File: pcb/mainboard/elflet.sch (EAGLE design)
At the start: 37 parts, among them J1 ZX62-B-5PA(33), J2 2212S-10SG-36, J3 STD-PINHD-1X6, Q1 IRLML6344TRPBF, Q2 ALS-PT19-315C_L177_TR8, SW1 SKRPACE010, U1 ESP-WROOM-32, U2 ADP3338AKCZ-3.3, U3 OSRB38C9AA, U4 BME280

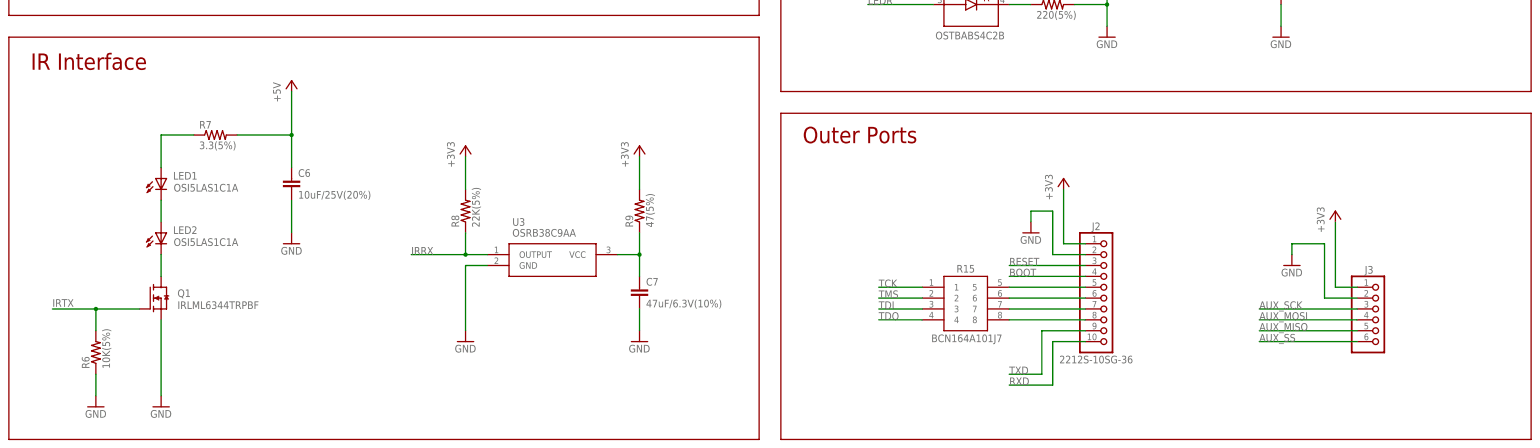
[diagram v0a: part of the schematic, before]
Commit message: place all parts on a board
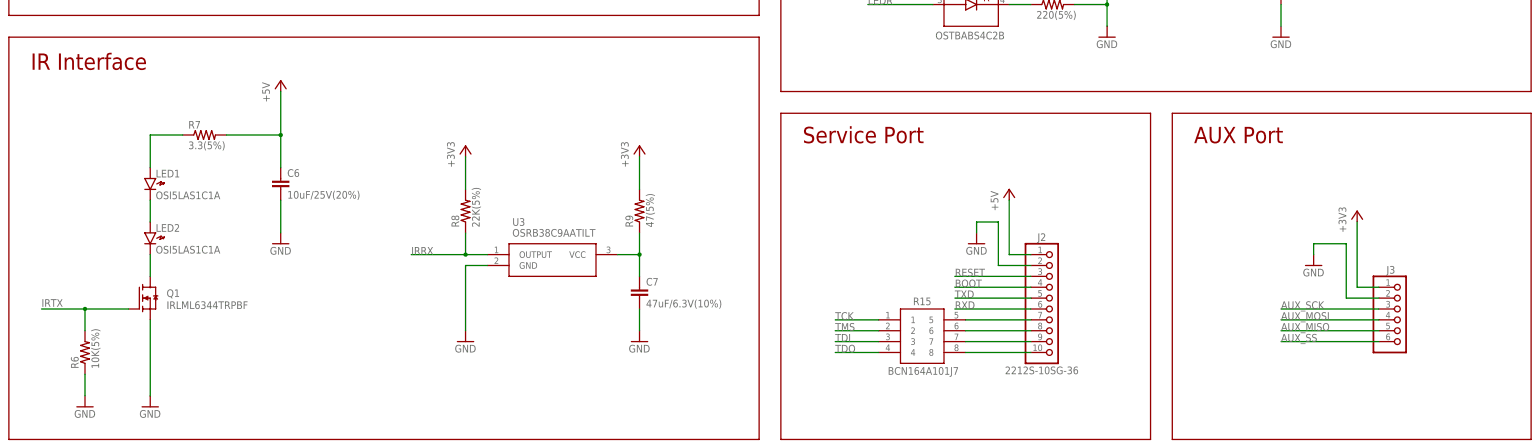
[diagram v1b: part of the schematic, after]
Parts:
- LED1, LED2: device led:LEDP-LCC-2 -> gen-discrete:LEDPLCC-2
- U3: value OSRB38C9AA -> OSRB38C9AATILT; device OSRB38C9AA:OSRB38C9AA -> OSRB38C9AA:OSRB38C9AATILT
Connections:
- net +3V3: no longer J2.1
- net +5V: now also J2.1
- net N$12: now also J2.10; no longer J2.8
- net N$2: now also LED1.K, LED2.A; no longer LED2.C, Q1.D
- net N$3: now also LED2.K, Q1.D; no longer LED1.C, LED2.A
- net N$6: now also J2.7; no longer J2.5
- net N$7: now also J2.8; no longer J2.6
- net N$8: now also J2.9; no longer J2.7
- net RXD: now also J2.6; no longer J2.10
- net TXD: now also J2.5; no longer J2.9
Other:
- note added: "AUX Port"
- note added: "Service Port"
- note removed: "Outer Ports"
- moved on the sheet: C6, J2, J3, Q1, R15, R6, R7

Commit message: initial wiring
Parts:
- Q2: value ALS-PT19-315C_L177_TR8 -> ALS-PT19-315C/L177/TR8
- R1, R10, R14, R2, R3: value 10K(5%) -> 10K(0.1%)
- R11, R12: value 33(5%) -> 33(0.1%)
- R13: value 220(5%) -> 220(0.1%)
- R15: value BCN164A101J7 -> BCN164AB101J7
- R4, R5: value 4.7K(5%) -> 4.7K(0.1%)
- R7: device rcl:R-US_R6332 -> gen-discrete:R-US_R2512
- R8: value 22K(5%) -> 22K(0.1%)
- R9: value 47(5%) -> 47(0.1%)
- U3: value OSRB38C9AATILT -> OSRB38C9AA
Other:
- moved on the sheet: U1
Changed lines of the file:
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@@
 <class number="0" name="default" width="0" drill="0">
 </class>
-<class number="1" name="gnd" width="0.6096" drill="0.2032">
+<class number="1" name="gnd" width="0.4572" drill="0.2032">
 </class>
-<class number="2" name="power" width="0.6096" drill="0.2032">
+<class number="2" name="power" width="0.4572" drill="0.2032">
+</class>
+<class number="3" name="irled" width="0.4572" drill="0.2032">
 </class>
 </classes>
@@
 <part name="+3V3" library="supply1" library_urn="urn:adsk.eagle:library:371" deviceset="+3V3" device=""/>
 <part name="GND4" library="supply1" library_urn="urn:adsk.eagle:library:371" deviceset="GND" device=""/>
-<part name="R1" library="rcl" library_urn="urn:adsk.eagle:library:334" deviceset="R-US_" device="R0805" package3d_urn="urn:adsk.eagle:package:23553/2" value="10K(5%)"/>
-<part name="R2" library="rcl" library_urn="urn:adsk.eagle:library:334" deviceset="R-US_" device="R0805" package3d_urn="urn:adsk.eagle:package:23553/2" value="10K(5%)"/>
+<part name="R1" library="rcl" library_urn="urn:adsk.eagle:library:334" deviceset="R-US_" device="R0805" package3d_urn="urn:adsk.eagle:package:23553/2" value="10K(0.1%)"/>
+<part name="R2" library="rcl" library_urn="urn:adsk.eagle:library:334" deviceset="R-US_" device="R0805" package3d_urn="urn:adsk.eagle:package:23553/2" value="10K(0.1%)"/>
 <part name="+3V4" library="supply1" library_urn="urn:adsk.eagle:library:371" deviceset="+3V3" device=""/>
-<part name="R3" library="rcl" library_urn="urn:adsk.eagle:library:334" deviceset="R-US_" device="R0805" package3d_urn="urn:adsk.eagle:package:23553/2" value="10K(5%)"/>
+<part name="R3" library="rcl" library_urn="urn:adsk.eagle:library:334" deviceset="R-US_" device="R0805" package3d_urn="urn:adsk.eagle:package:23553/2" value="10K(0.1%)"/>
 <part name="GND5" library="supply1" library_urn="urn:adsk.eagle:library:371" deviceset="GND" device=""/>
-<part name="R4" library="rcl" library_urn="urn:adsk.eagle:library:334" deviceset="R-US_" device="R0603" package3d_urn="urn:adsk.eagle:package:23555/2" value="4.7K(5%)"/>
-<part name="R5" library="rcl" library_urn="urn:adsk.eagle:library:334" deviceset="R-US_" device="R0603" package3d_urn="urn:adsk.eagle:package:23555/2" value="4.7K(5%)"/>
+<part name="R4" library="rcl" library_urn="urn:adsk.eagle:library:334" deviceset="R-US_" device="R0603" package3d_urn="urn:adsk.eagle:package:23555/2" value="4.7K(0.1%)"/>
+<part name="R5" library="rcl" library_urn="urn:adsk.eagle:library:334" deviceset="R-US_" device="R0603" package3d_urn="urn:adsk.eagle:package:23555/2" value="4.7K(0.1%)"/>
 <part name="+3V5" library="supply1" library_urn="urn:adsk.eagle:library:371" deviceset="+3V3" device=""/>
 <part name="J1" library="ZX62-B-5PA(33)" deviceset="ZX62-B-5PA(33)" device=""/>
@@
 <part name="R6" library="rcl" library_urn="urn:adsk.eagle:library:334" deviceset="R-US_" device="R0805" package3d_urn="urn:adsk.eagle:package:23553/2" value="10K(5%)"/>
 <part name="GND9" library="supply1" library_urn="urn:adsk.eagle:library:371" deviceset="GND" device=""/>
-<part name="R7" library="rcl" library_urn="urn:adsk.eagle:library:334" deviceset="R-US_" device="R6332" package3d_urn="urn:adsk.eagle:package:23559/2" value="3.3(5%)"/>
+<part name="R7" library="gen-discrete" deviceset="R-US_" device="R2512" package3d_urn="urn:adsk.eagle:package:23545/2" value="3.3(5%)"/>
 <part name="P+2" library="supply1" library_urn="urn:adsk.eagle:library:371" deviceset="+5V" device=""/>
 <part name="C6" library="rcl" library_urn="urn:adsk.eagle:library:334" deviceset="C-EU" device="C1608" package3d_urn="urn:adsk.eagle:package:23621/2" value="10uF/25V(20%)"/>
 <part name="GND10" library="supply1" library_urn="urn:adsk.eagle:library:371" deviceset="GND" device=""/>
-<part name="U3" library="OSRB38C9AA" deviceset="OSRB38C9AA" device="TILT" value="OSRB38C9AATILT"/>
+<part name="U3" library="OSRB38C9AA" deviceset="OSRB38C9AA" device="TILT" value="OSRB38C9AA"/>
 <part name="GND11" library="supply1" library_urn="urn:adsk.eagle:library:371" deviceset="GND" device=""/>
 <part name="+3V6" library="supply1" library_urn="urn:adsk.eagle:library:371" deviceset="+3V3" device=""/>
-<part name="R8" library="rcl" library_urn="urn:adsk.eagle:library:334" deviceset="R-US_" device="R0603" package3d_urn="urn:adsk.eagle:package:23555/2" value="22K(5%)"/>
+<part name="R8" library="rcl" library_urn="urn:adsk.eagle:library:334" deviceset="R-US_" device="R0603" package3d_urn="urn:adsk.eagle:package:23555/2" value="22K(0.1%)"/>
 <part name="+3V7" library="supply1" library_urn="urn:adsk.eagle:library:371" deviceset="+3V3" device=""/>
-<part name="R9" library="rcl" library_urn="urn:adsk.eagle:library:334" deviceset="R-US_" device="R0603" package3d_urn="urn:adsk.eagle:package:23555/2" value="47(5%)"/>
+<part name="R9" library="rcl" library_urn="urn:adsk.eagle:library:334" deviceset="R-US_" device="R0603" package3d_urn="urn:adsk.eagle:package:23555/2" value="47(0.1%)"/>
 <part name="C7" library="rcl" library_urn="urn:adsk.eagle:library:334" deviceset="C-EU" device="C3216" package3d_urn="urn:adsk.eagle:package:23628/2" value="47uF/6.3V(10%)"/>
 <part name="GND12" library="supply1" library_urn="urn:adsk.eagle:library:371" deviceset="GND" device=""/>
@@
 <part name="GND15" library="supply1" library_urn="urn:adsk.eagle:library:371" deviceset="GND" device=""/>
 <part name="+3V9" library="supply1" library_urn="urn:adsk.eagle:library:371" deviceset="+3V3" device=""/>
-<part name="Q2" library="ALS-PT19-315C_L177_TR8" deviceset="ALS-PT19-315C_L177_TR8" device=""/>
+<part name="Q2" library="ALS-PT19-315C_L177_TR8" deviceset="ALS-PT19-315C_L177_TR8" device="" value="ALS-PT19-315C/L177/TR8"/>
 <part name="+3V10" library="supply1" library_urn="urn:adsk.eagle:library:371" deviceset="+3V3" device=""/>
-<part name="R10" library="rcl" library_urn="urn:adsk.eagle:library:334" deviceset="R-US_" device="R0805" package3d_urn="urn:adsk.eagle:package:23553/2" value="10K(5%)"/>
+<part name="R10" library="rcl" library_urn="urn:adsk.eagle:library:334" deviceset="R-US_" device="R0805" package3d_urn="urn:adsk.eagle:package:23553/2" value="10K(0.1%)"/>
 <part name="GND16" library="supply1" library_urn="urn:adsk.eagle:library:371" deviceset="GND" device=""/>
 <part name="LED3" library="OSTBABS4C2B" deviceset="OSTBABS4C2B" device=""/>
-<part name="R11" library="rcl" library_urn="urn:adsk.eagle:library:334" deviceset="R-US_" device="R0805" package3d_urn="urn:adsk.eagle:package:23553/2" value="33(5%)"/>
-<part name="R12" library="rcl" library_urn="urn:adsk.eagle:library:334" deviceset="R-US_" device="R0805" package3d_urn="urn:adsk.eagle:package:23553/2" value="33(5%)"/>
-<part name="R13" library="rcl" library_urn="urn:adsk.eagle:library:334" deviceset="R-US_" device="R0805" package3d_urn="urn:adsk.eagle:package:23553/2" value="220(5%)"/>
+<part name="R11" library="rcl" library_urn="urn:adsk.eagle:library:334" deviceset="R-US_" device="R0805" package3d_urn="urn:adsk.eagle:package:23553/2" value="33(0.1%)"/>
+<part name="R12" library="rcl" library_urn="urn:adsk.eagle:library:334" deviceset="R-US_" device="R0805" package3d_urn="urn:adsk.eagle:package:23553/2" value="33(0.1%)"/>
+<part name="R13" library="rcl" library_urn="urn:adsk.eagle:library:334" deviceset="R-US_" device="R0805" package3d_urn="urn:adsk.eagle:package:23553/2" value="220(0.1%)"/>
 <part name="GND17" library="supply1" library_urn="urn:adsk.eagle:library:371" deviceset="GND" device=""/>
 <part name="SW1" library="SKRPACE010" deviceset="SKRPACE010" device=""/>
 <part name="+3V11" library="supply1" library_urn="urn:adsk.eagle:library:371" deviceset="+3V3" device=""/>
-<part name="R14" library="rcl" library_urn="urn:adsk.eagle:library:334" deviceset="R-US_" device="R0805" package3d_urn="urn:adsk.eagle:package:23553/2" value="10K(5%)"/>
+<part name="R14" library="rcl" library_urn="urn:adsk.eagle:library:334" deviceset="R-US_" device="R0805" package3d_urn="urn:adsk.eagle:package:23553/2" value="10K(0.1%)"/>
 <part name="GND18" library="supply1" library_urn="urn:adsk.eagle:library:371" deviceset="GND" device=""/>
 <part name="J2" library="connector" deviceset="STD-PINHD-1X10" device="" value="2212S-10SG-36"/>
 <part name="GND6" library="supply1" library_urn="urn:adsk.eagle:library:371" deviceset="GND" device=""/>
-<part name="R15" library="BCN164A102J7" deviceset="BCN164A102J7" device="" value="BCN164A101J7"/>
-<part name="J3" library="connector" deviceset="STD-PINHD-1X6" device="" value=""/>
+<part name="R15" library="BCN164A102J7" deviceset="BCN164A102J7" device="" value="BCN164AB101J7"/>
+<part name="J3" library="connector" deviceset="STD-PINHD-1X6" device="" value="STD-PINHD-1X6"/>
 <part name="+3V13" library="supply1" library_urn="urn:adsk.eagle:library:371" deviceset="+3V3" device=""/>
 <part name="GND19" library="supply1" library_urn="urn:adsk.eagle:library:371" deviceset="GND" device=""/>
@@
 </segment>
 </net>
-<net name="N$4" class="0">
+<net name="N$4" class="3">
 <segment>
 <pinref part="R7" gate="G$1" pin="1"/>
@@
 </segment>
 </net>
-<net name="N$2" class="0">
+<net name="N$2" class="3">
 <segment>
 <pinref part="LED1" gate="G$1" pin="K"/>
@@
 </segment>
 </net>
-<net name="N$3" class="0">
+<net name="N$3" class="3">
 <segment>
 <pinref part="LED2" gate="G$1" pin="K"/>
